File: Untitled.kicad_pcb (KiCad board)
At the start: 2 copper layers, 99.5 x 68.9 mm, 64 parts, among them J1 USB_B, U1 LD1117S33TR, U2 ESP32-WROOM, U3 TLC5926IDW, U4 TLC5926IDW, U5 TLC5926IDW

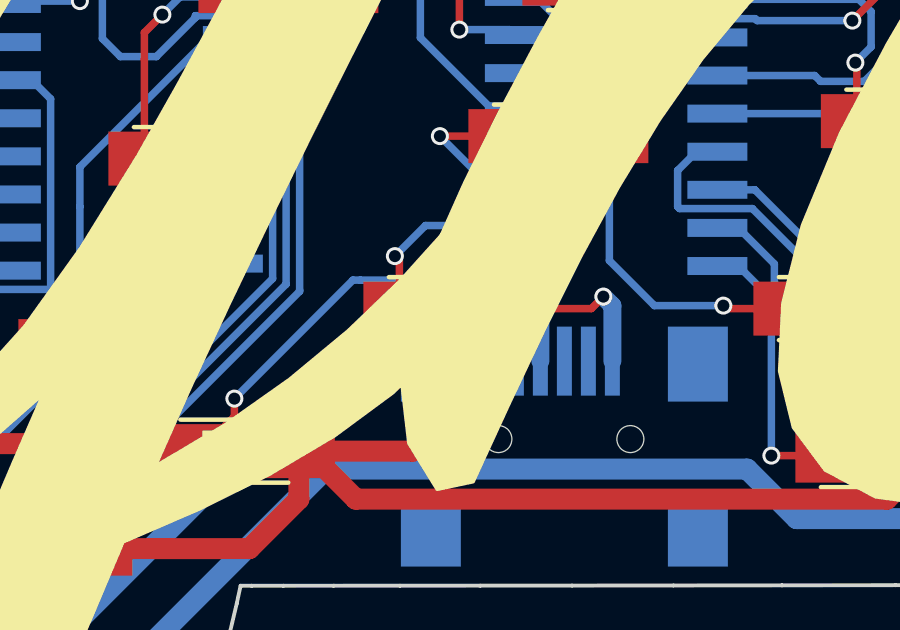
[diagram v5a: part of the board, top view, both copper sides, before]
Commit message: Fix for incorrect GND pad on mini usb connector
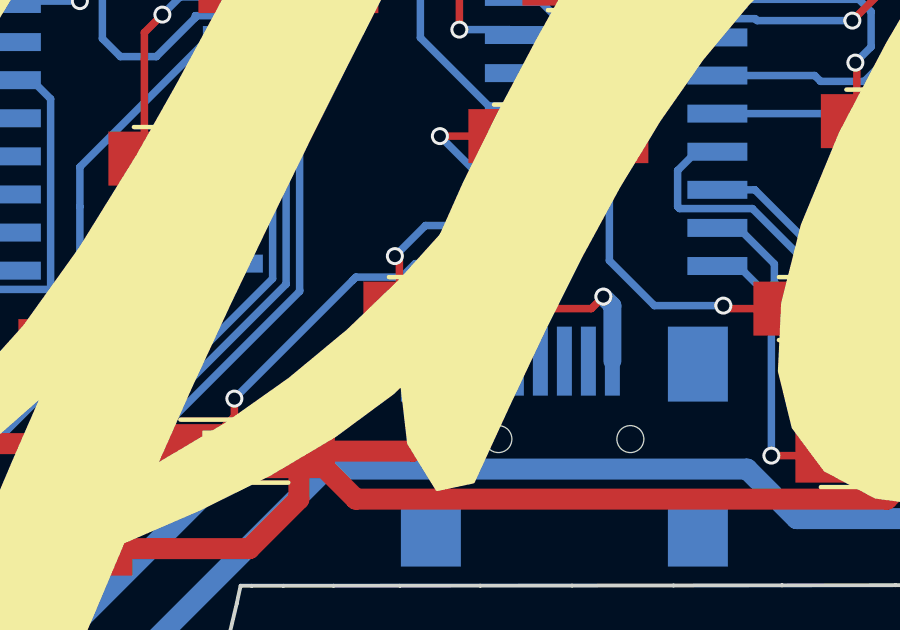
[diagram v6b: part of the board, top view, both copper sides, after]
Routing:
- net GND: track 284.1 -> 283.3 mm
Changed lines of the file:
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@@
     (mod_text_size 1 1)
     (mod_text_width 0.15)
-    (pad_size 0.7 2.5)
+    (pad_size 2.30124 0.50038)
     (pad_drill 0)
     (pad_to_mask_clearance 0.2)
@@
     (add_net GND)
   )
+  (module Connectors:USB_Mini-B (layer B.Cu)
+    (at 195.9 101.2 90)
+    (descr "USB Mini-B 5-pin SMD connector")
+    (tags "USB USB_B USB_Mini connector")
+    (attr smd)
+    (fp_text reference J1 (at 0 -6.90118 90) (layer B.SilkS)
+      (effects (font (size 1 1) (thickness 0.15)) (justify mirror))
+    )
+    (fp_text value USB_B (at 0 7.0993 90) (layer B.Fab)
+      (effects (font (size 1 1) (thickness 0.15)) (justify mirror))
+    )
+    (fp_line (start -4.85 5.7) (end 4.85 5.7) (layer B.CrtYd) (width 0.05))
+    (fp_line (start 4.85 5.7) (end 4.85 -5.7) (layer B.CrtYd) (width 0.05))
+    (fp_line (start 4.85 -5.7) (end -4.85 -5.7) (layer B.CrtYd) (width 0.05))
+    (fp_line (start -4.85 -5.7) (end -4.85 5.7) (layer B.CrtYd) (width 0.05))
+    (fp_line (start -3.59918 3.85064) (end -3.59918 -3.85064) (layer B.SilkS) (width 0.15))
+    (fp_line (start -4.59994 3.85064) (end -4.59994 -3.85064) (layer B.SilkS) (width 0.15))
+    (fp_line (start -4.59994 -3.85064) (end 4.59994 -3.85064) (layer B.SilkS) (width 0.15))
+    (fp_line (start 4.59994 -3.85064) (end 4.59994 3.85064) (layer B.SilkS) (width 0.15))
+    (fp_line (start 4.59994 3.85064) (end -4.59994 3.85064) (layer B.SilkS) (width 0.15))
+    (pad 1 smd rect (at 3.44932 1.6002 90) (size 2.30124 0.50038) (layers B.Cu B.Paste B.Mask)
+      (net 2 +5V))
+    (pad 2 smd rect (at 3.44932 0.8001 90) (size 2.30124 0.50038) (layers B.Cu B.Paste B.Mask)
+      (net 61 "Net-(J1-Pad2)"))
+    (pad 3 smd rect (at 3.44932 0 90) (size 2.30124 0.50038) (layers B.Cu B.Paste B.Mask)
+      (net 62 "Net-(J1-Pad3)"))
+    (pad 5 smd rect (at 3.44932 -0.8001 90) (size 2.30124 0.50038) (layers B.Cu B.Paste B.Mask)
+      (net 63 "Net-(J1-Pad5)"))
+    (pad 4 smd rect (at 3.44932 -1.6002 90) (size 2.30124 0.50038) (layers B.Cu B.Paste B.Mask)
+      (net 1 GND))
+    (pad 6 smd rect (at 3.35026 4.45008 90) (size 2.49936 1.99898) (layers B.Cu B.Paste B.Mask))
+    (pad 6 smd rect (at -2.14884 4.45008 90) (size 2.49936 1.99898) (layers B.Cu B.Paste B.Mask))
+    (pad 6 smd rect (at 3.35026 -4.45008 90) (size 2.49936 1.99898) (layers B.Cu B.Paste B.Mask))
+    (pad 6 smd rect (at -2.14884 -4.45008 90) (size 2.49936 1.99898) (layers B.Cu B.Paste B.Mask))
+    (pad "" np_thru_hole circle (at 0.8509 2.19964 90) (size 0.89916 0.89916) (drill 0.89916) (layers *.Cu *.Mask))
+    (pad "" np_thru_hole circle (at 0.8509 -2.19964 90) (size 0.89916 0.89916) (drill 0.89916) (layers *.Cu *.Mask))
+  )
   (module ESP32-footprints-Lib:ESP32-WROOM (layer B.Cu)
     (at 230.55 89.4 270)
@@
     )
   )
-  (module Connectors:USB_Mini-B (layer B.Cu)
-    (at 195.9 101.2 90)
-    (descr "USB Mini-B 5-pin SMD connector")
-    (tags "USB USB_B USB_Mini connector")
-    (attr smd)
-    (fp_text reference J1 (at 0 -6.90118 90) (layer B.SilkS)
-      (effects (font (size 1 1) (thickness 0.15)) (justify mirror))
-    )
-    (fp_text value USB_B (at 0 7.0993 90) (layer B.Fab)
-      (effects (font (size 1 1) (thickness 0.15)) (justify mirror))
-    )
-    (fp_line (start -4.85 5.7) (end 4.85 5.7) (layer B.CrtYd) (width 0.05))
-    (fp_line (start 4.85 5.7) (end 4.85 -5.7) (layer B.CrtYd) (width 0.05))
-    (fp_line (start 4.85 -5.7) (end -4.85 -5.7) (layer B.CrtYd) (width 0.05))
-    (fp_line (start -4.85 -5.7) (end -4.85 5.7) (layer B.CrtYd) (width 0.05))
-    (fp_line (start -3.59918 3.85064) (end -3.59918 -3.85064) (layer B.SilkS) (width 0.15))
-    (fp_line (start -4.59994 3.85064) (end -4.59994 -3.85064) (layer B.SilkS) (width 0.15))
-    (fp_line (start -4.59994 -3.85064) (end 4.59994 -3.85064) (layer B.SilkS) (width 0.15))
-    (fp_line (start 4.59994 -3.85064) (end 4.59994 3.85064) (layer B.SilkS) (width 0.15))
-    (fp_line (start 4.59994 3.85064) (end -4.59994 3.85064) (layer B.SilkS) (width 0.15))
-    (pad 1 smd rect (at 3.44932 1.6002 90) (size 2.30124 0.50038) (layers B.Cu B.Paste B.Mask)
-      (net 2 +5V))
-    (pad 2 smd rect (at 3.44932 0.8001 90) (size 2.30124 0.50038) (layers B.Cu B.Paste B.Mask)
-      (net 61 "Net-(J1-Pad2)"))
-    (pad 3 smd rect (at 3.44932 0 90) (size 2.30124 0.50038) (layers B.Cu B.Paste B.Mask)
-      (net 62 "Net-(J1-Pad3)"))
-    (pad 4 smd rect (at 3.44932 -0.8001 90) (size 2.30124 0.50038) (layers B.Cu B.Paste B.Mask)
-      (net 1 GND))
-    (pad 5 smd rect (at 3.44932 -1.6002 90) (size 2.30124 0.50038) (layers B.Cu B.Paste B.Mask)
-      (net 63 "Net-(J1-Pad5)"))
-    (pad 6 smd rect (at 3.35026 4.45008 90) (size 2.49936 1.99898) (layers B.Cu B.Paste B.Mask))
-    (pad 6 smd rect (at -2.14884 4.45008 90) (size 2.49936 1.99898) (layers B.Cu B.Paste B.Mask))
-    (pad 6 smd rect (at 3.35026 -4.45008 90) (size 2.49936 1.99898) (layers B.Cu B.Paste B.Mask))
-    (pad 6 smd rect (at -2.14884 -4.45008 90) (size 2.49936 1.99898) (layers B.Cu B.Paste B.Mask))
-    (pad "" np_thru_hole circle (at 0.8509 2.19964 90) (size 0.89916 0.89916) (drill 0.89916) (layers *.Cu *.Mask))
-    (pad "" np_thru_hole circle (at 0.8509 -2.19964 90) (size 0.89916 0.89916) (drill 0.89916) (layers *.Cu *.Mask))
-  )
   (module Housings_SOIC:SOIC-24W_7.5x15.4mm_Pitch1.27mm (layer B.Cu)
     (at 172.75 87.75 180)
@@
     (arrow2b (pts (xy 244.047502 144.801514) (xy 242.921585 145.389061)))
   )
+  (segment (start 194.2998 97.75068) (end 194.2998 96.10006) (width 0.5) (layer B.Cu) (net 1))
+  (segment (start 194.2998 96.10006) (end 193.82475 95.62501) (width 0.7) (layer B.Cu) (net 1))
+  (segment (start 193.82475 95.62501) (end 190.47499 95.62501) (width 0.7) (layer B.Cu) (net 1))
+  (segment (start 190.47499 95.62501) (end 190.37499 95.72501) (width 0.5) (layer B.Cu) (net 1))
+  (segment (start 179.150001 106.949999) (end 190.37499 95.72501) (width 0.7) (layer B.Cu) (net 1))
+  (segment (start 179.150001 114.749999) (end 179.150001 106.949999) (width 0.7) (layer B.Cu) (net 1))
+  (segment (start 179 114.9) (end 179.150001 114.749999) (width 0.7) (layer B.Cu) (net 1))
+  (segment (start 179 116.6) (end 179 114.9) (width 0.7) (layer B.Cu) (net 1))
   (segment (start 165.378523 102.7) (end 165.378523 108.648669) (width 0.7) (layer B.Cu) (net 1))
   (segment (start 165.378523 108.648669) (end 160.8 113.227192) (width 0.7) (layer B.Cu) (net 1))
@@
   (segment (start 237.8 102.3) (end 237.8 100.4) (width 0.7) (layer B.Cu) (net 1))
   (segment (start 237.8 100.4) (end 235.8 98.4) (width 0.7) (layer B.Cu) (net 1))
-  (segment (start 195.0999 96.04992) (end 195.0999 97.75068) (width 0.6) (layer B.Cu) (net 1))
-  (segment (start 194.77499 95.72501) (end 195.0999 96.04992) (width 0.7) (layer B.Cu) (net 1))
-  (segment (start 195.0999 96.04992) (end 195.0999 96.159968) (width 0.6) (layer B.Cu) (net 1))
-  (segment (start 179 116.6) (end 179 114.9) (width 0.7) (layer B.Cu) (net 1))
-  (segment (start 179 114.9) (end 179.150001 114.749999) (width 0.7) (layer B.Cu) (net 1))
-  (segment (start 190.37499 95.72501) (end 194.77499 95.72501) (width 0.7) (layer B.Cu) (net 1))
-  (segment (start 179.150001 114.749999) (end 179.150001 106.949999) (width 0.7) (layer B.Cu) (net 1))
-  (segment (start 179.150001 106.949999) (end 190.37499 95.72501) (width 0.7) (layer B.Cu) (net 1))
   (segment (start 179 116.6) (end 179 116.85) (width 0.25) (layer B.Cu) (net 1))
   (segment (start 210.4 80.61) (end 210.4 80.06) (width 0.25) (layer B.Cu) (net 1))
@@
   (segment (start 190.4 94.4) (end 190.25 94.25) (width 0.25) (layer F.Cu) (net 33))
   (via (at 190.25 94.25) (size 0.6) (drill 0.4) (layers F.Cu B.Cu) (net 33))
-  (segment (start 189.1 95.05) (end 193 95.05) (width 0.25) (layer B.Cu) (net 34))
-  (segment (start 188.85 95.05) (end 189.1 95.05) (width 0.25) (layer B.Cu) (net 34))
+  (segment (start 194.25 94.5) (end 190.925002 94.5) (width 0.25) (layer B.Cu) (net 34))
+  (segment (start 190.925002 94.5) (end 190.475002 94.95) (width 0.25) (layer B.Cu) (net 34))
+  (segment (start 190.475002 94.95) (end 188.95 94.95) (width 0.25) (layer B.Cu) (net 34))
+  (segment (start 188.95 94.95) (end 188.85 95.05) (width 0.25) (layer B.Cu) (net 34))
   (segment (start 184.9 99) (end 188.85 95.05) (width 0.25) (layer B.Cu) (net 34))
   (segment (start 183.45 100.75) (end 183.74957 100.75) (width 0.25) (layer F.Cu) (net 34))
@@
   (segment (start 183.74957 100.75) (end 184.9 99.59957) (width 0.25) (layer F.Cu) (net 34))
   (segment (start 184.9 99.59957) (end 184.9 99) (width 0.25) (layer F.Cu) (net 34))
-  (segment (start 193 95.05) (end 193.55 94.5) (width 0.25) (layer B.Cu) (net 34))
-  (segment (start 193.55 94.5) (end 194.25 94.5) (width 0.25) (layer B.Cu) (net 34))
   (segment (start 184.85 94.5) (end 184.85 95.4) (width 0.25) (layer B.Cu) (net 35))
   (segment (start 184.85 95.4) (end 178 102.25) (width 0.25) (layer B.Cu) (net 35))
